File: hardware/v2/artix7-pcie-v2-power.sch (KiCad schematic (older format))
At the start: 40 parts, among them U3 LP5907MFX, U5 TPS82130SILT, U6 TPS82150SILT, U7 TPS82150SILT, U8 TPS82130SILT, U9 TPS82150SILT

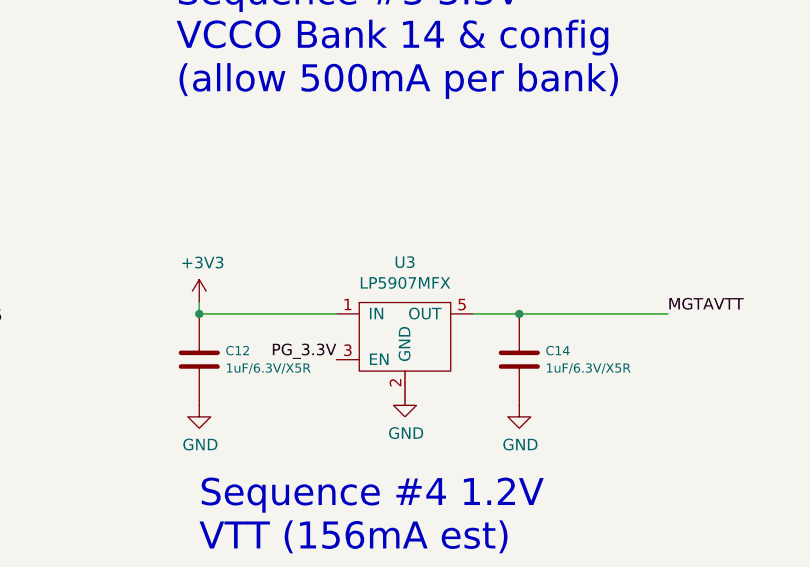
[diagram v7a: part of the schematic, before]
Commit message: v2 hardware: Aug2020/rc2 version - flip tx/rx pairs on s2 - add lcsc part numbers
rc2 errata schematic
- change serial port connector to add +3.3V ? (8-pin)(NO)
- add test points for flash pre-programming
- smaller package on input direction diodes (NO)
- bom dupe errors
- remove all p/s 0R bringup parts
- optimise bom (use 1.5k for led, 10k/4.7k for i2c pullups)
- done led is bright (change to 4.7k)
- improve shield grounding with RC
- check actual values of RGB resistors
- remove caps from clock inputs

rc2 errata pcb
- no gnd marking on serial port connector pins
- change serial port connector to add +3.3V ? (8-pin) (NO)
- no test points for flash pre-programming
- missing caps on xtal? (No but select xtal carefully)
- Cfg sel pins on clock chip?
- No silk on test points
- No +/- pair numbering on silk
- vcc test points for clk pre-programming? (or use bootloader)
- random silk circle under S2
- smaller package on input direction diodes (NO)
- no polarity on 100uF tantalum
- some via in or close to pads
- wrong button package (change from feather to chinese)
- gnd/vcc labels swapped at high end of J2
- clock chip OUT0_SEL_I2CB needs to be tied high after programming
- check teardrops
- power diode footprint marking reverse
- LEDs use cap footprint
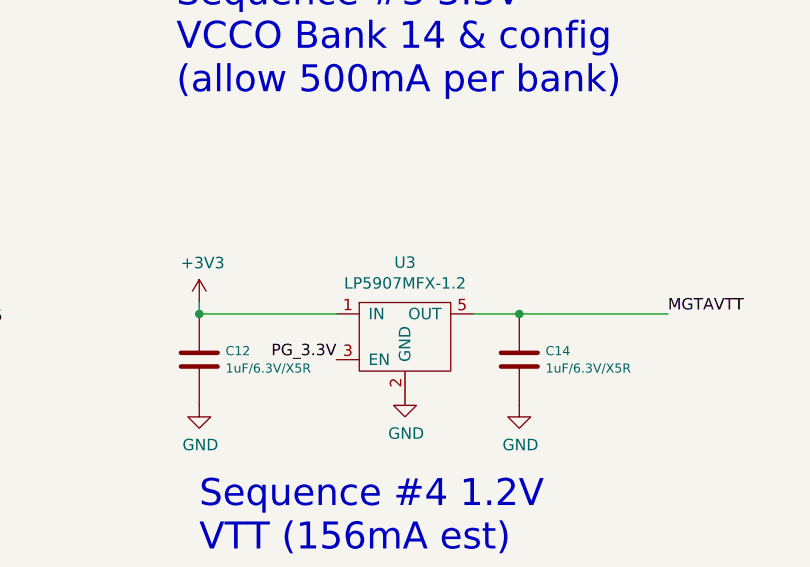
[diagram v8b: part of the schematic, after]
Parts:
- C10, C35, C36, C39, C7: footprint tom-passives:C_1206_3216Metric -> tom-passives:C_0805_2012Metric; LCSC (none) -> C45783
- C11, C13, C37, C5, C8: LCSC (none) -> C13585
- C12, C14: LCSC (none) -> C52923
- C15, C16, C38, C6, C9: LCSC (none) -> C26404
- R12, R13, R16, R17, R22, R23, R24, R25, R36, R38: LCSC (none) -> C25741
- R14: LCSC (none) -> C25874
- R18: LCSC (none) -> C11489
- R31, R32: LCSC (none) -> C36777
- R39: LCSC (none) -> C25777
- R40, R41: LCSC (none) -> C21189
- U3: value LP5907MFX -> LP5907MFX-1.2; LCSC (none) -> C73478
- U5, U6, U7, U8, U9: LCSC (none) -> DNP
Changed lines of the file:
@@
 P 9300 4250
 F 0 "U3" H 9300 4575 50  0000 C CNN
-F 1 "LP5907MFX" H 9300 4484 50  0000 C CNN
+F 1 "LP5907MFX-1.2" H 9300 4484 50  0000 C CNN
 F 2 "tom-semiconductors:SOT-23-5" H 9300 4250 50  0001 C CNN
 F 3 "http://www.ti.com/lit/ds/symlink/lp5907.pdf" H 9300 4250 50  0001 C CNN
 F 4 "296-39062-1-ND" H 9300 4250 50  0001 C CNN "Vendor"
+F 5 "C73478" H 9300 4250 50  0001 C CNN "LCSC"
 	1    9300 4250
 	1    0    0    -1
@@
 F 2 "tom-passives:C_0402_1005Metric" H 8438 4200 30  0001 C CNN
 F 3 "" H 8400 4350 60  0000 C CNN
+F 4 "C52923" H 8400 4350 50  0001 C CNN "LCSC"
 	1    8400 4350
 	1    0    0    -1
@@
 F 2 "tom-passives:C_0402_1005Metric" H 9838 4200 30  0001 C CNN
 F 3 "" H 9800 4350 60  0000 C CNN
+F 4 "C52923" H 9800 4350 50  0001 C CNN "LCSC"
 	1    9800 4350
 	1    0    0    -1
@@
 F 4 "C3216X7R1E106M160AE" H 950 1550 50  0001 C CNN "MFGPN"
 F 5 "399-8153-1-ND" H 950 1550 50  0001 C CNN "Vendor"
+F 6 "C13585" H 950 1550 50  0001 C CNN "LCSC"
 	1    950  1550
 	1    0    0    1
@@
 F 3 "" H 1400 2050 60  0001 C CNN
 F 4 "490-3248-1-ND" H 1400 2050 50  0001 C CNN "Vendor"
+F 5 "C26404" H 1400 2050 50  0001 C CNN "LCSC"
 	1    1400 2050
 	1    0    0    1
@@
 F 2 "tom-passives:R_0402_1005Metric" V 2930 2100 30  0001 C CNN
 F 3 "" H 3000 2100 30  0001 C CNN
+F 4 "C25741" H 3000 2100 50  0001 C CNN "LCSC"
 	1    3000 2100
 	1    0    0    -1
@@
 F 3 "" H 3250 1750 30  0001 C CNN
 F 4 "RMCF0402FT24K9CT-ND" H 3250 1750 50  0001 C CNN "Vendor"
+F 5 "C25874" H 3250 1750 50  0001 C CNN "LCSC"
 	1    3250 1750
 	0    -1   -1   0
@@
 F 2 "tom-passives:R_0402_1005Metric" H 3071 974 30  0001 L CNN
 F 3 "" H 3000 1050 30  0001 C CNN
+F 4 "C25741" H 3000 1050 50  0001 C CNN "LCSC"
 	1    3000 1050
 	1    0    0    -1
@@
 F 0 "C7" H 3615 1988 40  0000 L CNN
 F 1 "22uF/6.3V/X7S" H 3615 1912 40  0000 L CNN
-F 2 "tom-passives:C_1206_3216Metric" H 3538 1800 30  0001 C CNN
+F 2 "tom-passives:C_0805_2012Metric" H 3538 1800 30  0001 C CNN
 F 3 "" H 3500 1950 60  0001 C CNN
 F 4 "C2012X7S1A226M125AC" H 3500 1950 50  0001 C CNN "MFGPN"
 F 5 "1276-1771-1-ND" H 3500 1950 50  0001 C CNN "Vendor"
+F 6 "C45783" H 3500 1950 50  0001 C CNN "LCSC"
 	1    3500 1950
 	1    0    0    -1
@@
 F 4 "C3216X7R1E106M160AE" H 4400 1550 50  0001 C CNN "MFGPN"
 F 5 "399-8153-1-ND" H 4400 1550 50  0001 C CNN "Vendor"
+F 6 "C13585" H 4400 1550 50  0001 C CNN "LCSC"
 	1    4400 1550
 	1    0    0    1
@@
 F 3 "" H 4850 2050 60  0001 C CNN
 F 4 "490-3248-1-ND" H 4850 2050 50  0001 C CNN "Vendor"
+F 5 "C26404" H 4850 2050 50  0001 C CNN "LCSC"
 	1    4850 2050
 	1    0    0    1
@@
 F 2 "tom-passives:R_0402_1005Metric" V 6380 2100 30  0001 C CNN
 F 3 "" H 6450 2100 30  0001 C CNN
+F 4 "C25741" H 6450 2100 50  0001 C CNN "LCSC"
 	1    6450 2100
 	1    0    0    -1
@@
 F 3 "" H 6700 1750 30  0001 C CNN
 F 4 "2019-RK73H1ETTP1243FCT-ND" H 6700 1750 50  0001 C CNN "Vendor"
+F 5 "C36777" H 6700 1750 50  0001 C CNN "LCSC"
 	1    6700 1750
 	0    -1   -1   0
@@
 F 2 "tom-passives:R_0402_1005Metric" H 6521 974 30  0001 L CNN
 F 3 "" H 6450 1050 30  0001 C CNN
+F 4 "C25741" H 6450 1050 50  0001 C CNN "LCSC"
 	1    6450 1050
 	1    0    0    -1
@@
 F 0 "C35" H 7065 1988 40  0000 L CNN
 F 1 "22uF/6.3V/X7S" H 7065 1912 40  0000 L CNN
-F 2 "tom-passives:C_1206_3216Metric" H 6988 1800 30  0001 C CNN
+F 2 "tom-passives:C_0805_2012Metric" H 6988 1800 30  0001 C CNN
 F 3 "" H 6950 1950 60  0001 C CNN
 F 4 "C2012X7S1A226M125AC" H 6950 1950 50  0001 C CNN "MFGPN"
 F 5 "1276-1771-1-ND" H 6950 1950 50  0001 C CNN "Vendor"
+F 6 "C45783" H 6950 1950 50  0001 C CNN "LCSC"
 	1    6950 1950
 	1    0    0    -1
@@
 F 3 "http://www.ti.com/lit/ds/symlink/tps82130.pdf" H 9250 1701 60  0001 C CNN
 F 4 "296-47090-1-ND" H 8450 1400 50  0001 C CNN "Vendor"
+F 5 "DNP" H 8450 1400 50  0001 C CNN "LCSC"
 	1    8450 1400
 	1    0    0    -1
@@
 F 4 "C3216X7R1E106M160AE" H 8000 1550 50  0001 C CNN "MFGPN"
 F 5 "399-8153-1-ND" H 8000 1550 50  0001 C CNN "Vendor"
+F 6 "C13585" H 8000 1550 50  0001 C CNN "LCSC"
 	1    8000 1550
 	1    0    0    1
@@
 F 3 "" H 8450 2050 60  0001 C CNN
 F 4 "490-3248-1-ND" H 8450 2050 50  0001 C CNN "Vendor"
+F 5 "C26404" H 8450 2050 50  0001 C CNN "LCSC"
 	1    8450 2050
 	1    0    0    1
@@
 F 2 "tom-passives:R_0402_1005Metric" V 9980 2100 30  0001 C CNN
 F 3 "" H 10050 2100 30  0001 C CNN
+F 4 "C25741" H 10050 2100 50  0001 C CNN "LCSC"
 	1    10050 2100
 	1    0    0    -1
@@
 F 3 "" H 10300 1750 30  0001 C CNN
 F 4 "738-RMCF0402FT316KCT-ND" H 10300 1750 50  0001 C CNN "Vendor"
+F 5 "C25777" H 10300 1750 50  0001 C CNN "LCSC"
 	1    10300 1750
 	0    -1   -1   0
@@
 F 0 "C39" H 10665 1988 40  0000 L CNN
 F 1 "22uF/6.3V/X7S" H 10665 1912 40  0000 L CNN
-F 2 "tom-passives:C_1206_3216Metric" H 10588 1800 30  0001 C CNN
+F 2 "tom-passives:C_0805_2012Metric" H 10588 1800 30  0001 C CNN
 F 3 "" H 10550 1950 60  0001 C CNN
 F 4 "C2012X7S1A226M125AC" H 10550 1950 50  0001 C CNN "MFGPN"
 F 5 "1276-1771-1-ND" H 10550 1950 50  0001 C CNN "Vendor"
+F 6 "C45783" H 10550 1950 50  0001 C CNN "LCSC"
 	1    10550 1950
 	1    0    0    -1
@@
 F 3 "http://www.ti.com/lit/ds/symlink/tps82130.pdf" H 2200 4451 60  0001 C CNN
 F 4 "296-47090-1-ND" H 1400 4150 50  0001 C CNN "Vendor"
+F 5 "DNP" H 1400 4150 50  0001 C CNN "LCSC"
 	1    1400 4150
 	1    0    0    -1
@@
 F 4 "C3216X7R1E106M160AE" H 950 4300 50  0001 C CNN "MFGPN"
 F 5 "399-8153-1-ND" H 950 4300 50  0001 C CNN "Vendor"
+F 6 "C13585" H 950 4300 50  0001 C CNN "LCSC"
 	1    950  4300
 	1    0    0    1
@@
 F 3 "" H 1400 4800 60  0001 C CNN
 F 4 "490-3248-1-ND" H 1400 4800 50  0001 C CNN "Vendor"
+F 5 "C26404" H 1400 4800 50  0001 C CNN "LCSC"
 	1    1400 4800
 	1    0    0    1
@@
 F 2 "tom-passives:R_0402_1005Metric" V 2930 4850 30  0001 C CNN
 F 3 "" H 3000 4850 30  0001 C CNN
+F 4 "C25741" H 3000 4850 50  0001 C CNN "LCSC"
 	1    3000 4850
 	1    0    0    -1
@@
 F 3 "" H 3250 4500 30  0001 C CNN
 F 4 "RMCF0402FT215KCT-ND" H 3250 4500 50  0001 C CNN "Vendor"
+F 5 "C11489" H 3250 4500 50  0001 C CNN "LCSC"
 	1    3250 4500
 	0    -1   -1   0
@@
 F 2 "tom-passives:R_0402_1005Metric" H 3071 3724 30  0001 L CNN
 F 3 "" H 3000 3800 30  0001 C CNN
+F 4 "C25741" H 3000 3800 50  0001 C CNN "LCSC"
 	1    3000 3800
 	1    0    0    -1
@@
 F 0 "C10" H 3615 4738 40  0000 L CNN
 F 1 "22uF/6.3V/X7S" H 3615 4662 40  0000 L CNN
-F 2 "tom-passives:C_1206_3216Metric" H 3538 4550 30  0001 C CNN
+F 2 "tom-passives:C_0805_2012Metric" H 3538 4550 30  0001 C CNN
 F 3 "" H 3500 4700 60  0001 C CNN
 F 4 "C2012X7S1A226M125AC" H 3500 4700 50  0001 C CNN "MFGPN"
 F 5 "1276-1771-1-ND" H 3500 4700 50  0001 C CNN "Vendor"
+F 6 "C45783" H 3500 4700 50  0001 C CNN "LCSC"
 	1    3500 4700
 	1    0    0    -1
@@
 F 3 "http://www.ti.com/lit/ds/symlink/tps82130.pdf" H 5650 4451 60  0001 C CNN
 F 4 "296-47436-1-ND" H 4850 4150 50  0001 C CNN "Vendor"
+F 5 "DNP" H 4850 4150 50  0001 C CNN "LCSC"
 	1    4850 4150
 	1    0    0    -1
@@
 F 4 "C3216X7R1E106M160AE" H 4400 4300 50  0001 C CNN "MFGPN"
 F 5 "399-8153-1-ND" H 4400 4300 50  0001 C CNN "Vendor"
+F 6 "C13585" H 4400 4300 50  0001 C CNN "LCSC"
 	1    4400 4300
 	1    0    0    1
@@
 F 3 "" H 4850 4800 60  0001 C CNN
 F 4 "490-3248-1-ND" H 4850 4800 50  0001 C CNN "Vendor"
+F 5 "C26404" H 4850 4800 50  0001 C CNN "LCSC"
 	1    4850 4800
 	1    0    0    1
@@
 F 2 "tom-passives:R_0402_1005Metric" V 6380 4850 30  0001 C CNN
 F 3 "" H 6450 4850 30  0001 C CNN
+F 4 "C25741" H 6450 4850 50  0001 C CNN "LCSC"
 	1    6450 4850
 	1    0    0    -1
@@
 F 3 "" H 6700 4500 30  0001 C CNN
 F 4 "2019-RK73H1ETTP1243FCT-ND" H 6700 4500 50  0001 C CNN "Vendor"
+F 5 "C36777" H 6700 4500 50  0001 C CNN "LCSC"
 	1    6700 4500
 	0    -1   -1   0
@@
 F 2 "tom-passives:R_0402_1005Metric" H 6521 3724 30  0001 L CNN
 F 3 "" H 6450 3800 30  0001 C CNN
+F 4 "C25741" H 6450 3800 50  0001 C CNN "LCSC"
 	1    6450 3800
 	1    0    0    -1
@@
 F 0 "C36" H 7065 4738 40  0000 L CNN
 F 1 "22uF/6.3V/X7S" H 7065 4662 40  0000 L CNN
-F 2 "tom-passives:C_1206_3216Metric" H 6988 4550 30  0001 C CNN
+F 2 "tom-passives:C_0805_2012Metric" H 6988 4550 30  0001 C CNN
 F 3 "" H 6950 4700 60  0001 C CNN
 F 4 "C2012X7S1A226M125AC" H 6950 4700 50  0001 C CNN "MFGPN"
 F 5 "1276-1771-1-ND" H 6950 4700 50  0001 C CNN "Vendor"
+F 6 "C45783" H 6950 4700 50  0001 C CNN "LCSC"
 	1    6950 4700
 	1    0    0    -1
@@
 F 2 "tom-passives:R_0603_1608Metric_NoPaste" H 1921 6874 30  0001 L CNN
 F 3 "" H 1850 6950 30  0001 C CNN
+F 4 "C21189" H 1850 6950 50  0001 C CNN "LCSC"
 	1    1850 6950
 	0    1    1    0
@@
 F 2 "tom-passives:R_0603_1608Metric_NoPaste" H 2271 6674 30  0001 L CNN
 F 3 "" H 2200 6750 30  0001 C CNN
+F 4 "C21189" H 2200 6750 50  0001 C CNN "LCSC"
 	1    2200 6750
 	0    1    1    0
@@
 F 3 "http://www.ti.com/lit/ds/symlink/tps82130.pdf" H 5650 1701 60  0001 C CNN
 F 4 "296-47090-1-ND" H 4850 1400 50  0001 C CNN "Vendor"
+F 5 "DNP" H 4850 1400 50  0001 C CNN "LCSC"
 	1    4850 1400
 	1    0    0    -1
@@
 F 3 "http://www.ti.com/lit/ds/symlink/tps82130.pdf" H 2200 1701 60  0001 C CNN
 F 4 "296-47436-1-ND" H 1400 1400 50  0001 C CNN "Vendor"
+F 5 "DNP" H 1400 1400 50  0001 C CNN "LCSC"
 	1    1400 1400
 	1    0    0    -1
@@
 F 2 "tom-passives:R_0402_1005Metric" H 10121 974 30  0001 L CNN
 F 3 "" H 10050 1050 30  0001 C CNN
+F 4 "C25741" H 10050 1050 50  0001 C CNN "LCSC"
 	1    10050 1050
 	1    0    0    -1
